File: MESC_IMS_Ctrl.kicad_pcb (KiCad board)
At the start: 2 copper layers, 100 x 75 mm, 220 parts, among them J1 Conn_01x08_Female, J10 Conn_01x04_Male, J2 Conn_01x08_Female, J3 Conn_01x08_Female, J4 Conn_01x06_Male, J5 Conn_ARM_JTAG_SWD_10, J6 USB_C_Receptacle_USB2.0, J7 Conn_01x03_Male, J8 Conn_01x04_Male, J9 Conn_01x08_Male, U1 STM32F303CBTx, U10 TPS61041DBV, U2 LM5017MR, U3 TPS76333, U4 INA240A1PW, U5 UCC21520DW, U6 INA240A1PW, U7 UCC21520DW, U8 INA240A1PW, U9 UCC21520DW, Y1 ASE-8.000MHZ-LC-T

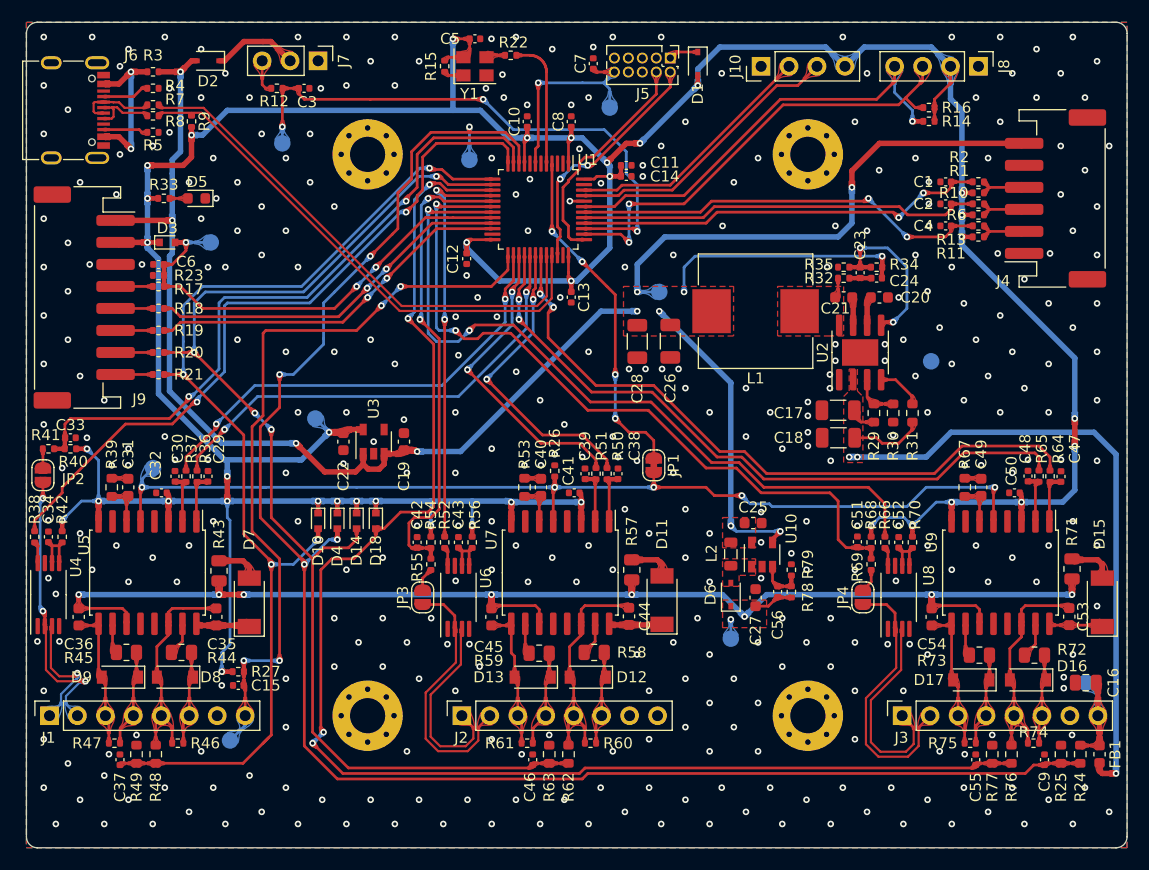
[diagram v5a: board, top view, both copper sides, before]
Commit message: upgrading to 4layer
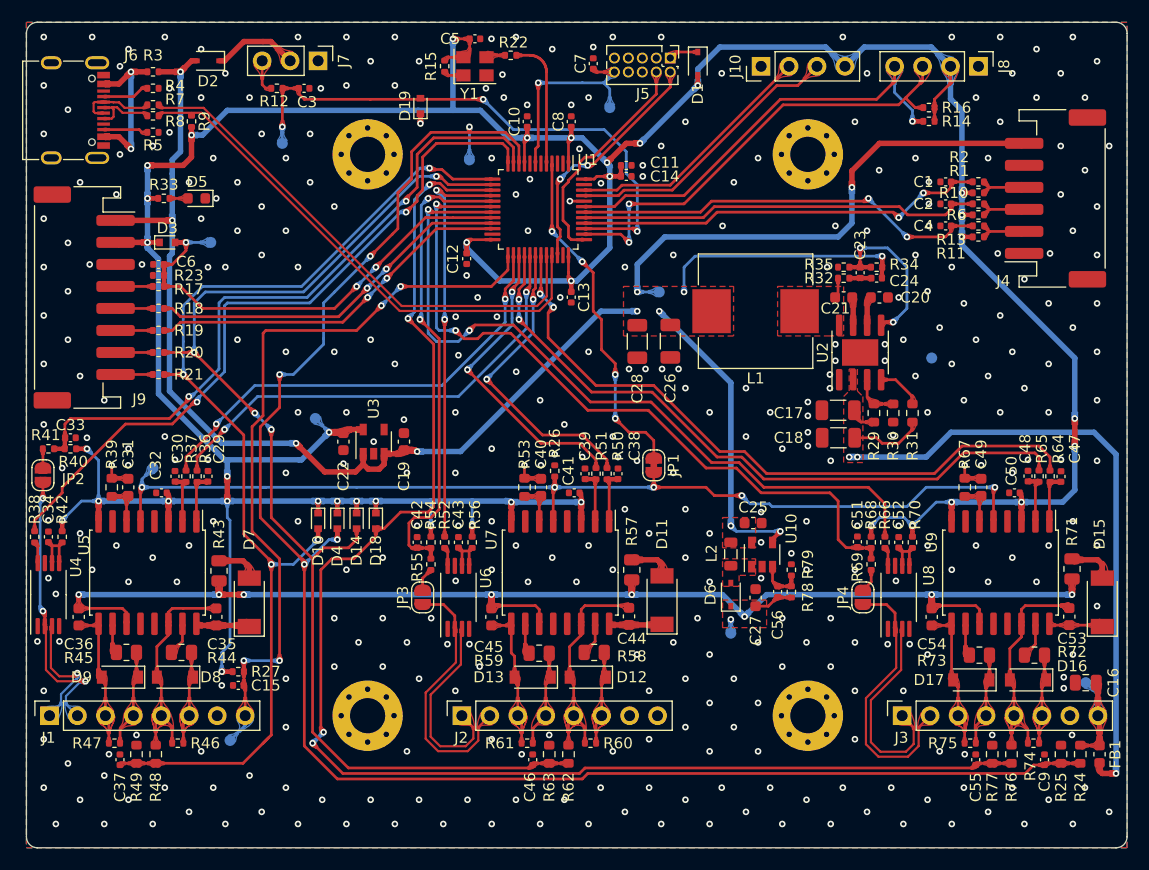
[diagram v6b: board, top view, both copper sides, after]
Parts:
- added D19: BAT41KFILM, Diode_SMD:D_SOD-523, F.Cu at (144.8, 82.6)
- added svg2mod: G***, label, B.Cu at (157.0, 97.0)
- added svg2mod: G***, label, B.Cu at (151.6, 93.8)
- R46, R47, R60, R61, R74, R75: value 39k -> 100k
- TP1, TP10, TP11, TP2, TP3, TP4, TP5, TP6, TP7, TP8, TP9: footprint TestPoint:TestPoint_Pad_D1.5mm -> TestPoint:TestPoint_Pad_D1.0mm
- moved TP9 0.50 mm to (173.0, 130.5)
- moved TP11 0.30 mm to (191.2, 105.5)
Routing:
- net GND: track 5.85 -> 9.37 mm
- net +3V3: track 365.7 -> 367.8 mm, vias 38 -> 39
- net VDD: track 122.0 -> 121.5 mm
- added copper zone on B.Cu, net +3V3
- added copper zone on In1.Cu, net GND
- added copper zone on In2.Cu, net GND
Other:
- copper layers 2 -> 4
